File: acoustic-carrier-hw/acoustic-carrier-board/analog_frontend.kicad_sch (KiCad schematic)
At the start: 56 parts, among them J1 8P8C_Shielded, J10 BWU.FL-IPEX1, J11 BWU.FL-IPEX1, J5 BWU.FL-IPEX1, J7 BWU.FL-IPEX1, U13 TL432DBZ, U2 THS4521IDGK, U3 DGQ2788AEN-T1-GE4, U5 LMV321

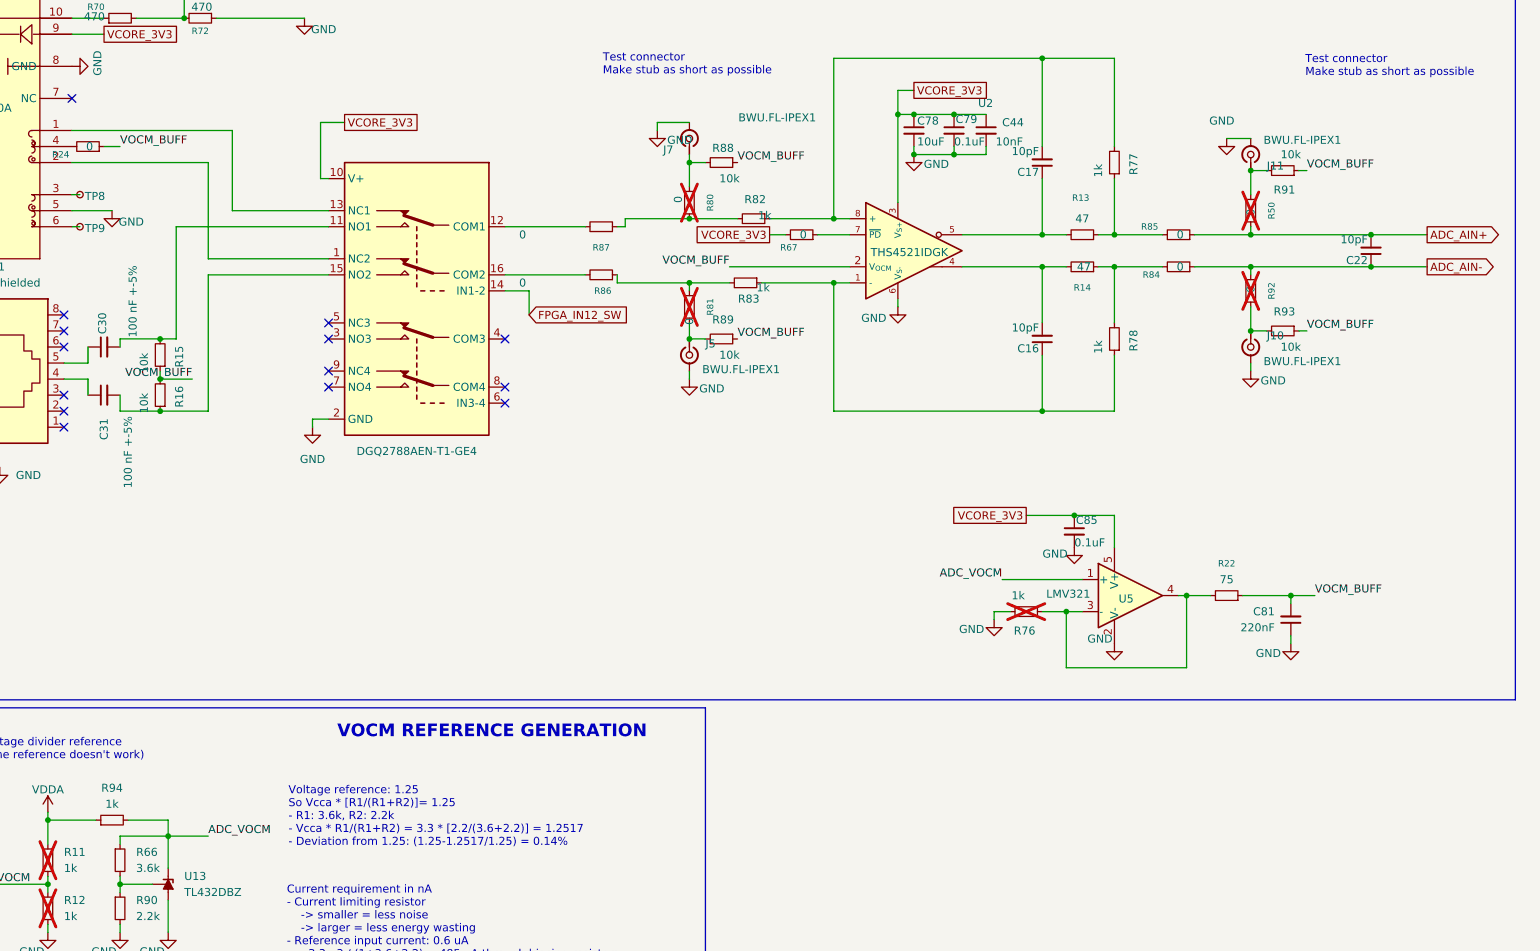
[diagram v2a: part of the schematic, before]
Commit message: [carrier] Fixed minor symbol errors, added minor routing info (next) continue schematic check
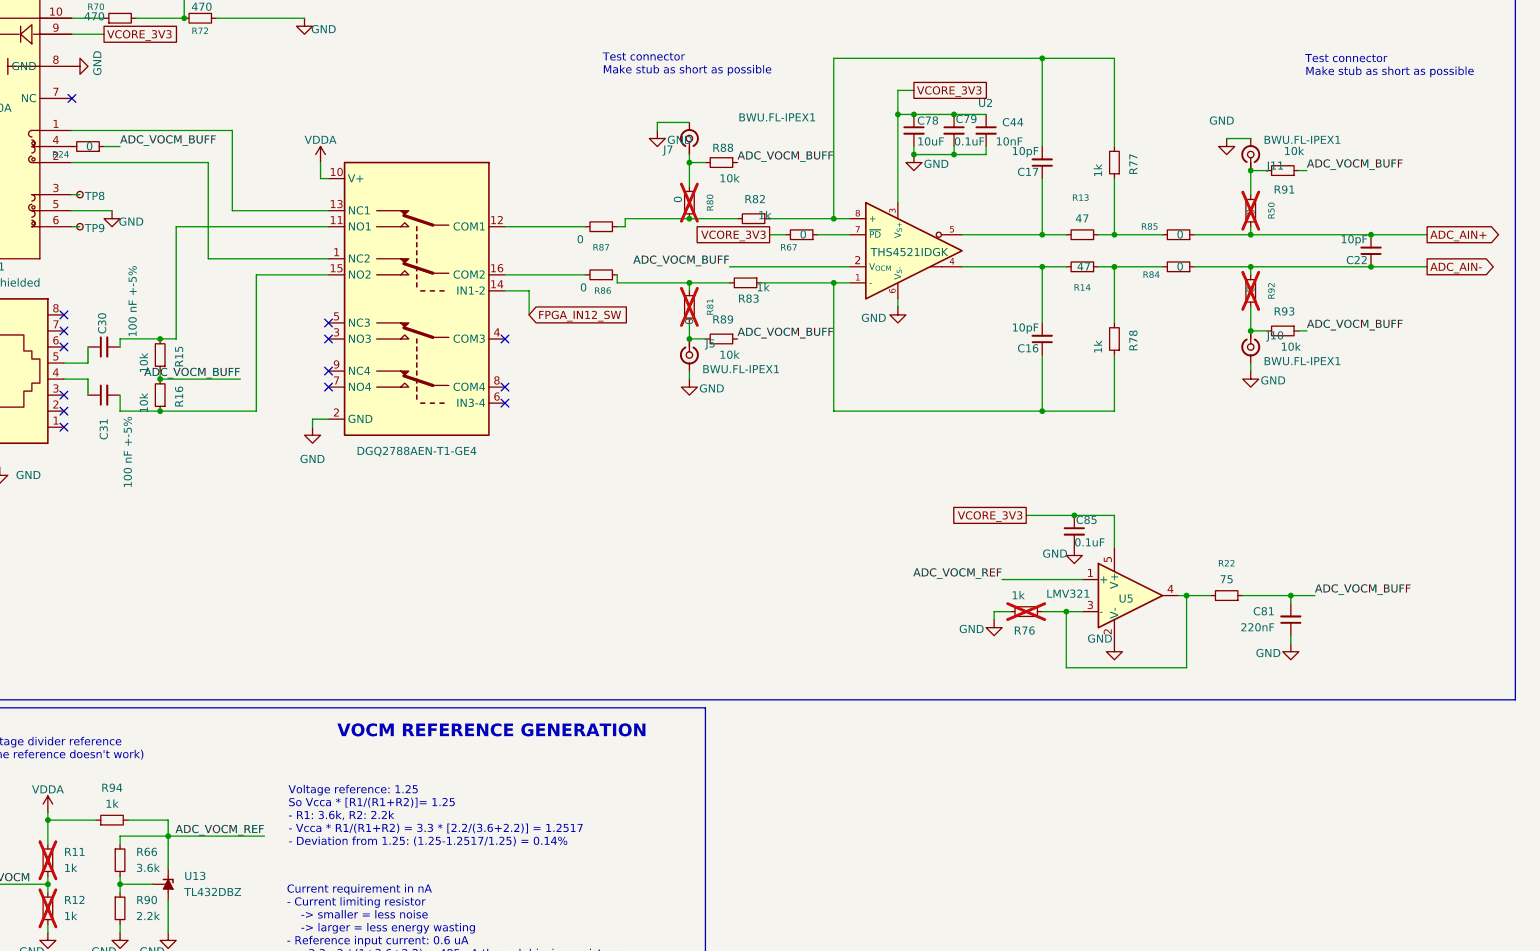
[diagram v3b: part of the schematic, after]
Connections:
- net ADC_VOCM: no longer R66.1, R94.2, U13.2 (K), U5.1 (+)
- net VCORE_3V3: no longer U3.10 (V+)
- net VDDA: now also U3.10 (V+)
- net VOCM_BUFF renamed ADC_VOCM_BUFF
- new net ADC_VOCM_REF: R66.1, R94.2, U13.2 (K), U5.1 (+)
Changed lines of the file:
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@@
 	(wire
 		(pts
-			(xy 68.58 96.52) (xy 76.2 96.52)
-		)
-		(stroke
-			(width 0)
-			(type default)
-		)
-	)
-	(wire
-		(pts
 			(xy 92.71 99.06) (xy 92.71 97.79)
 		)
@@
 	(wire
 		(pts
-			(xy 68.58 91.44) (xy 73.66 91.44)
+			(xy 68.58 91.44) (xy 81.28 91.44)
 		)
 		(stroke
@@
 	(wire
 		(pts
-			(xy 76.2 74.93) (xy 76.2 96.52)
+			(xy 83.82 74.93) (xy 83.82 96.52)
 		)
 		(stroke
@@
 	(wire
 		(pts
-			(xy 76.2 74.93) (xy 95.25 74.93)
-		)
-		(stroke
-			(width 0)
-			(type default)
-		)
-	)
-	(wire
-		(pts
 			(xy 53.34 88.9) (xy 57.15 88.9)
 		)
@@
 	(wire
 		(pts
-			(xy 93.98 50.8) (xy 93.98 59.69)
+			(xy 93.98 57.15) (xy 93.98 59.69)
 		)
 		(stroke
@@
 	(wire
 		(pts
-			(xy 69.85 163.83) (xy 76.2 163.83)
+			(xy 69.85 163.83) (xy 85.09 163.83)
 		)
 		(stroke
@@
 	(wire
 		(pts
+			(xy 83.82 74.93) (xy 95.25 74.93)
+		)
+		(stroke
+			(width 0)
+			(type default)
+		)
+	)
+	(wire
+		(pts
 			(xy 57.15 88.9) (xy 57.15 86.36)
 		)
@@
 	(wire
 		(pts
-			(xy 97.79 50.8) (xy 93.98 50.8)
-		)
-		(stroke
-			(width 0)
-			(type default)
-		)
-	)
-	(wire
-		(pts
 			(xy 62.23 171.45) (xy 62.23 172.72)
 		)
@@
 	(wire
 		(pts
+			(xy 68.58 96.52) (xy 83.82 96.52)
+		)
+		(stroke
+			(width 0)
+			(type default)
+		)
+	)
+	(wire
+		(pts
 			(xy 212.09 128.27) (xy 214.63 128.27)
 		)
@@
 		)
 	)
-	(label "VOCM_BUFF"
+	(label "ADC_VOCM_BUFF"
 		(at 158.75 73.66 180)
 		(effects
@@
 		)
 	)
-	(label "VOCM_BUFF"
+	(label "ADC_VOCM_BUFF"
 		(at 62.23 54.61 0)
 		(effects
@@
 		)
 	)
-	(label "ADC_VOCM"
-		(at 76.2 163.83 0)
+	(label "ADC_VOCM_BUFF"
+		(at 160.02 57.15 0)
 		(effects
 			(font
@@
 		)
 	)
-	(label "VOCM_BUFF"
+	(label "ADC_VOCM_BUFF"
 		(at 251.46 125.73 0)
 		(effects
@@
 		)
 	)
-	(label "VOCM_BUFF"
+	(label "ADC_VOCM_BUFF"
 		(at 250.19 58.42 0)
 		(effects
@@
 		)
 	)
-	(label "VOCM_BUFF"
-		(at 160.02 57.15 0)
+	(label "ADC_VOCM_BUFF"
+		(at 81.28 91.44 180)
 		(effects
 			(font
 				(size 1.27 1.27)
 			)
-			(justify left bottom)
+			(justify right bottom)
 		)
 	)
-	(label "VOCM_BUFF"
-		(at 73.66 91.44 180)
+	(label "ADC_VOCM"
+		(at 38.1 171.45 0)
 		(effects
 			(font
 				(size 1.27 1.27)
 			)
-			(justify right bottom)
+			(justify left bottom)
 		)
 	)
-	(label "ADC_VOCM"
-		(at 38.1 171.45 0)
+	(label "ADC_VOCM_REF"
+		(at 85.09 163.83 180)
 		(effects
 			(font
 				(size 1.27 1.27)
 			)
-			(justify left bottom)
+			(justify right bottom)
 		)
 	)
-	(label "ADC_VOCM"
+	(label "ADC_VOCM_REF"
 		(at 201.93 123.19 180)
 		(effects
@@
 		)
 	)
-	(label "VOCM_BUFF"
+	(label "ADC_VOCM_BUFF"
 		(at 250.19 83.82 0)
 		(effects
@@
 		)
 	)
-	(label "VOCM_BUFF"
+	(label "ADC_VOCM_BUFF"
 		(at 160.02 85.09 0)
 		(effects
@@
 		)
 	)
-	(global_label "VCORE_3V3"
-		(shape passive)
-		(at 97.79 50.8 0)
-		(fields_autoplaced yes)
-		(effects
-			(font
-				(size 1.27 1.27)
-			)
-			(justify left)
-		)
-		(property "Intersheetrefs" "${INTERSHEET_REFS}"
-			(at 110.2472 50.8 0)
-			(effects
-				(font
-					(size 1.27 1.27)
-				)
-				(justify left)
-				(hide yes)
-			)
-		)
-	)
 	(symbol
 		(lib_id "power:GND")
@@
 	)
 	(symbol
+		(lib_id "power:VDDA")
+		(at 93.98 57.15 0)
+		(unit 1)
+		(exclude_from_sim no)
+		(in_bom yes)
+		(on_board yes)
+		(dnp no)
+		(property "Reference" "#PWR0117"
+			(at 93.98 60.96 0)
+			(effects
+				(font
+					(size 1.27 1.27)
+				)
+				(hide yes)
+			)
+		)
+		(property "Value" "VDDA"
+			(at 93.98 53.594 0)
+			(effects
+				(font
+					(size 1.27 1.27)
+				)
+			)
+		)
+		(property "Footprint" ""
+			(at 93.98 57.15 0)
+			(effects
+				(font
+					(size 1.27 1.27)
+				)
+				(hide yes)
+			)
+		)
+		(property "Datasheet" ""
+			(at 93.98 57.15 0)
+			(effects
+				(font
+					(size 1.27 1.27)
+				)
+				(hide yes)
+			)
+		)
+		(property "Description" "Power symbol creates a global label with name \"VDDA\""
+			(at 93.98 57.15 0)
+			(effects
+				(font
+					(size 1.27 1.27)
+				)
+				(hide yes)
+			)
+		)
+		(pin "1"
+		)
+		(instances
+			(project "acoustic-carrier-board"
+				(path "/25b015c9-ab13-4427-b72c-b6f348597100/2e3c577d-8737-43a3-b422-36e75ce65de9"
+					(reference "#PWR0117")
+					(unit 1)
+				)
+			)
+		)
+	)
+	(symbol
 		(lib_id "Device:R_Small")
 		(at 74.93 26.67 90)
@@
 		)
 		(property "Value" "10k"
-			(at 247.65 55.88 90)
+			(at 248.158 55.372 90)
 			(effects
 				(font
@@
 		)
 		(property "Value" "0"
-			(at 125.984 68.58 90)
+			(at 135.128 69.342 90)
 			(effects
 				(font
@@
 		)
 		(property "Value" "0"
-			(at 125.984 76.2 90)
+			(at 135.636 76.962 90)
 			(effects
 				(font

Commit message: [carrier] Review of adc_connections-page done
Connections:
- net FPGA_ADC_LED0 renamed FPGA_LED0
- net FPGA_ADC_LED1 renamed FPGA_LED1
- net FPGA_IN12_SW renamed ADC_IN12_SW
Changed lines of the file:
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@@
 		)
 	)
-	(global_label "FPGA_ADC_LED1"
+	(global_label "FPGA_LED1"
 		(shape input)
 		(at 66.04 20.32 0)
@@
 		)
 		(property "Intersheetrefs" "${INTERSHEET_REFS}"
-			(at 83.9628 20.32 0)
+			(at 79.3666 20.32 0)
 			(effects
 				(font
@@
 		)
 	)
-	(global_label "FPGA_ADC_LED0"
+	(global_label "FPGA_LED0"
 		(shape input)
 		(at 72.39 29.21 0)
@@
 		)
 		(property "Intersheetrefs" "${INTERSHEET_REFS}"
-			(at 90.3128 29.21 0)
+			(at 85.7166 29.21 0)
 			(effects
 				(font
@@
 		)
 	)
-	(global_label "FPGA_IN12_SW"
+	(global_label "ADC_IN12_SW"
 		(shape input)
 		(at 127 81.28 0)
@@
 		)
 		(property "Intersheetrefs" "${INTERSHEET_REFS}"
-			(at 143.6528 81.28 0)
+			(at 142.5642 81.28 0)
 			(effects
 				(font

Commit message: [carrier] Did additional tests with tina-ti and blocking cap, did schematic check up to adc input buffer
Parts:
- removed C31: 100 nF +-5%, Capacitor_SMD:C_0603_1608Metric_Pad1.08x0.95mm_HandSolder, symbol Device:C_Small
- added C25: 100 nF +-5%, Capacitor_SMD:C_0603_1608Metric_Pad1.08x0.95mm_HandSolder, symbol Device:C_Small
- added J12, J13, J14: BWU.FL-IPEX1, fpga:BWU.FL-IPEX1, symbol Connector:Conn_Coaxial_Small
- added TP10, TP11, TP12: TestPoint_Small, TestPoint:TestPoint_Pad_D1.5mm, symbol Connector:TestPoint_Small
- R17: value 0 +-1% -> 0; footprint Resistor_SMD:R_0805_2012Metric_Pad1.20x1.40mm_HandSolder -> Resistor_SMD:R_0603_1608Metric_Pad0.98x0.95mm_HandSolder; LPN 0805W8F0000T5E -> C21189; MPN C17477 -> 0603WAF0000T5E
- R66: value 3.6k -> 1.5k; LPN 0603WAF3601T5E -> 0603WAF1501T5E; MPN C22980 -> C22843
- R90: value 2.2k -> 4.7k; LPN C4190 -> C23162; MPN 0603WAF2201T5E -> 0603WAF4701T5E
- RJ1: LCSC Part C163507 -> (none)
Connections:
- net ADC_VOCM is gone; now on net ADC_VOCM_REF: R11.2, R12.1
- net GND: now also J12.2 (Ext), J13.2 (Ext), J14.2 (Ext)
- net at R16.1, U3.15 (NO2): now also C25.2
- net at U3.3 (NO3): now also J13.1 (In)
- net at U3.4 (COM3): now also J14.1 (In)
- net at U3.5 (NC3): now also J12.1 (In)
- net at U3.6 (IN3-4): now also TP12.1
- net at J1.1: now also TP10.1
- net at J1.2: now also TP11.1
- net at J1.4: now also C25.1
- no-connect marks 14 -> 8
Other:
- note added: "ADC CONNECTORS"
- note added: "ADC INPUT BUFFER"
- note added: "ADC LOW PASS FILTER"
- note added: "ADC SWITCH"
- note added: "Current requirement in nA - Current limiting resistor -> smaller = less noise -> larger = less energy wasting - Reference input current: 0.6 uA - 3.3e-3 / (1+1.5+4.7) = 532 uA through biasing resistors - (3.3-1.65) / 1k = 1.65 mA flowing through the Cathode"
- note added: "VOCM REFERENCE BUFFERING"
- note added: "Voltage reference: 1.25 Target voltage: 1.65 So Vtarget * [R1/(R1+R2)]= Vref - R1: 1.5k, R2: 4.6k - Vref * R1/(R1+R2) = Vtarget * [4.6/(1.5+4.6)] = Vref - Deviation from 1.25: (1.25-1.244/1.25) = 0.48%"
- note removed: "ADC FRONTEND"
- note removed: "Current requirement in nA - Current limiting resistor -> smaller = less noise -> larger = less energy wasting - Reference input current: 0.6 uA - 3.3e-3 / (1+3.6+2.2) = 485 uA through biasing resistors - (3.3-1.65) / 1k = 1.65 mA flowing through the Cathode"
- note removed: "Voltage reference: 1.25 So Vcca * [R1/(R1+R2)]= 1.25 - R1: 3.6k, R2: 2.2k - Vcca * R1/(R1+R2) = 3.3 * [2.2/(3.6+2.2)] = 1.2517 - Deviation from 1.25: (1.25-1.2517/1.25) = 0.14%"
- moved on the sheet: C16, C17, C30, C44, C78, C79, C81, C85, J1, J5, J7, R11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

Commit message: [carrier] analog frontend check DONE, (next) check config and boot-flash pin connections
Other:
- note added: "- Ethernet magnetics by default for decoupling Layout of transition between 2 ADC-inputs: - Use 0-ohm resistor to cross lower trace (instead of jumpers for signal integrity) LEDS: - Current through leds (3.3 - 2.2) / 2e3 = 0.55 mA (voltage drop 1.8-2.8 V) - Differential impedance: 100 ohms - Input capacitance: 100 nF, f_plateau = 1/[2*pi*C*(R_diff/2)] = 30 kHz Pin 13, 14: shield / frame connection"
- note added: "ADC Filter - Optimize later with signal generator + measurements - Input impedance (max 100 kOhm) >>> then source (100 ohm)"
- note removed: "- Ethernet magnetics by default for decoupling - 0 ohm resistor in series for LC damping purposes (single-ended use) - Alternative input with DC-blocking capacitors with RJ45 Layout of transition between 2 ADC-inputs: - Use 0-ohm resistor to cross lower trace (instead of jumpers for signal integrity) Make sure the 0-ohm resistors and jumpers come together at the same spot LEDS: - Current through 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"
- note removed: "ADC Filter - Rudimentary prototyping with LTSpice + TI design note - Optimize later with signal generator + measurements - Input impedance (max 100 kOhm) >>> then source (100 ohm) ADC 0 ohm resistance - Series - possibility to switch to single-ended, short AIN- - Damping on AIN+ - Parallel - Possible footprint to common mode - THS4521 should drive a symmetric load - One option: leave it open - Se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"
- note removed: "Max offst: 4% <<<< 1' @ 1 MHz - Added 0-ohm series resistor in case of single-ended operation (LC damping) p8: center tap with capacitor in between (bob-smith)"
- moved on the sheet: C22, J10, J11, J5, J7, R50, R80, R81, R83, R84, R85, R88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
